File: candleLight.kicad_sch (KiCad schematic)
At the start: 43 parts, among them J1 USB_C_Receptacle_USB2.0, J2 Conn_Phoenix, J3 Conn_SWD, J4 Conn_IO, J5 Conn_BOOT0, J6 Conn_CAN_Jumper, J7 Conn_5V, U1 STM32F072C8Tx, U2 AMS1117-3.3, U3 TJA1051TK-3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

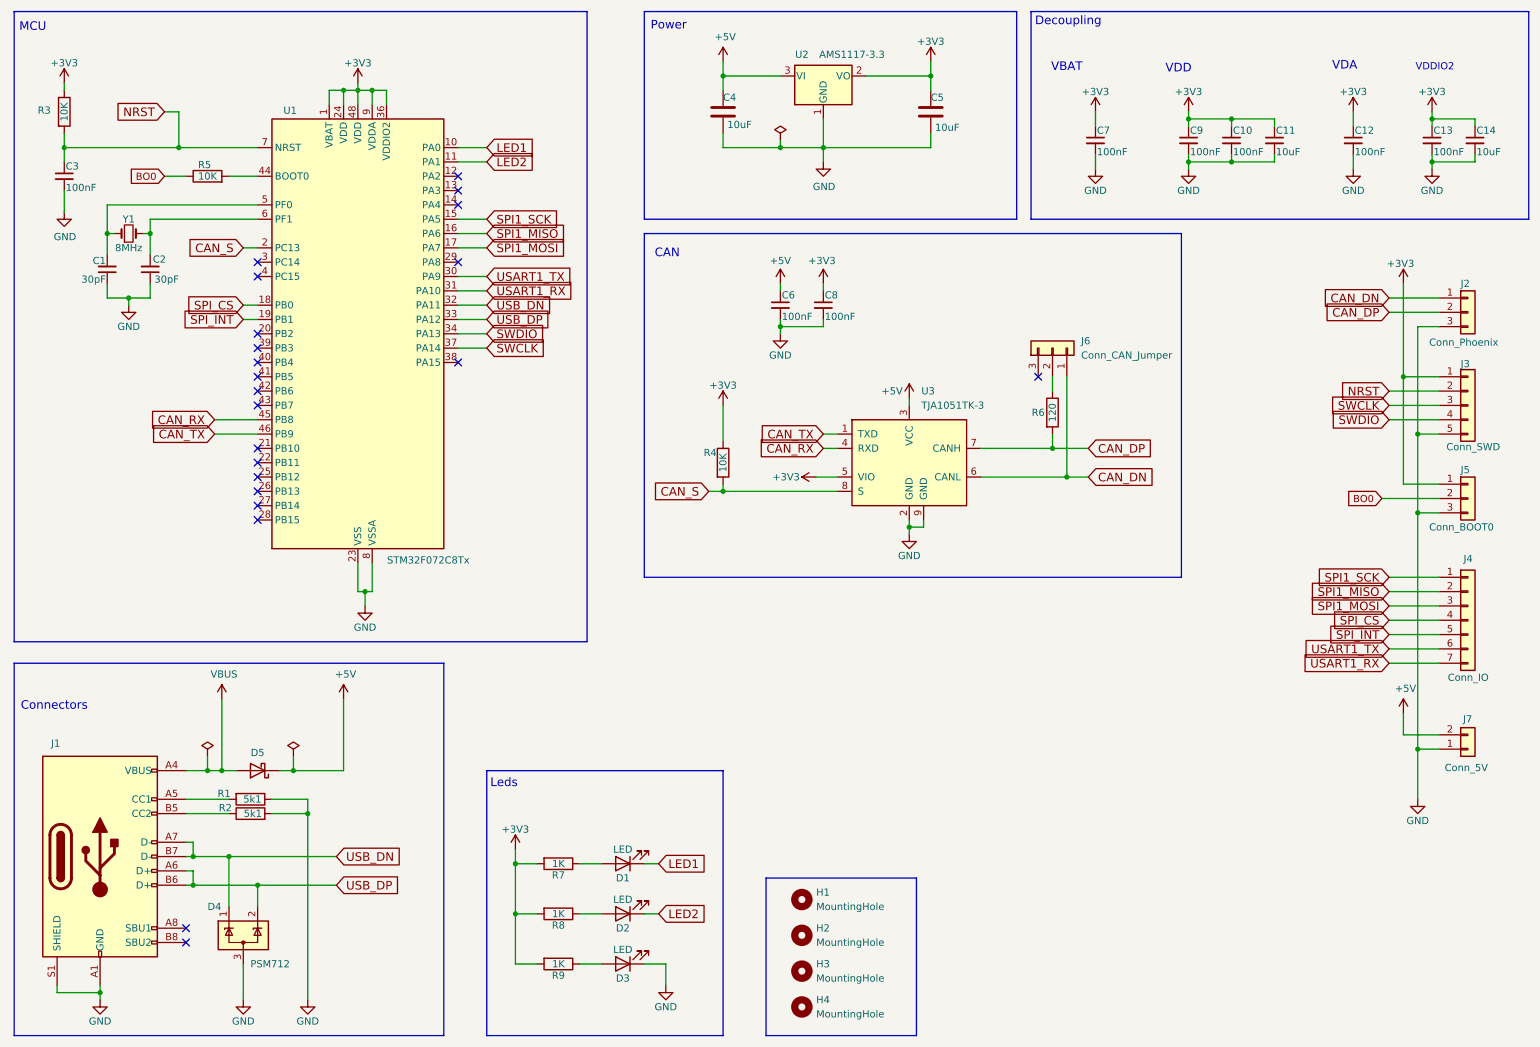
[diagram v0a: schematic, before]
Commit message: update schematic
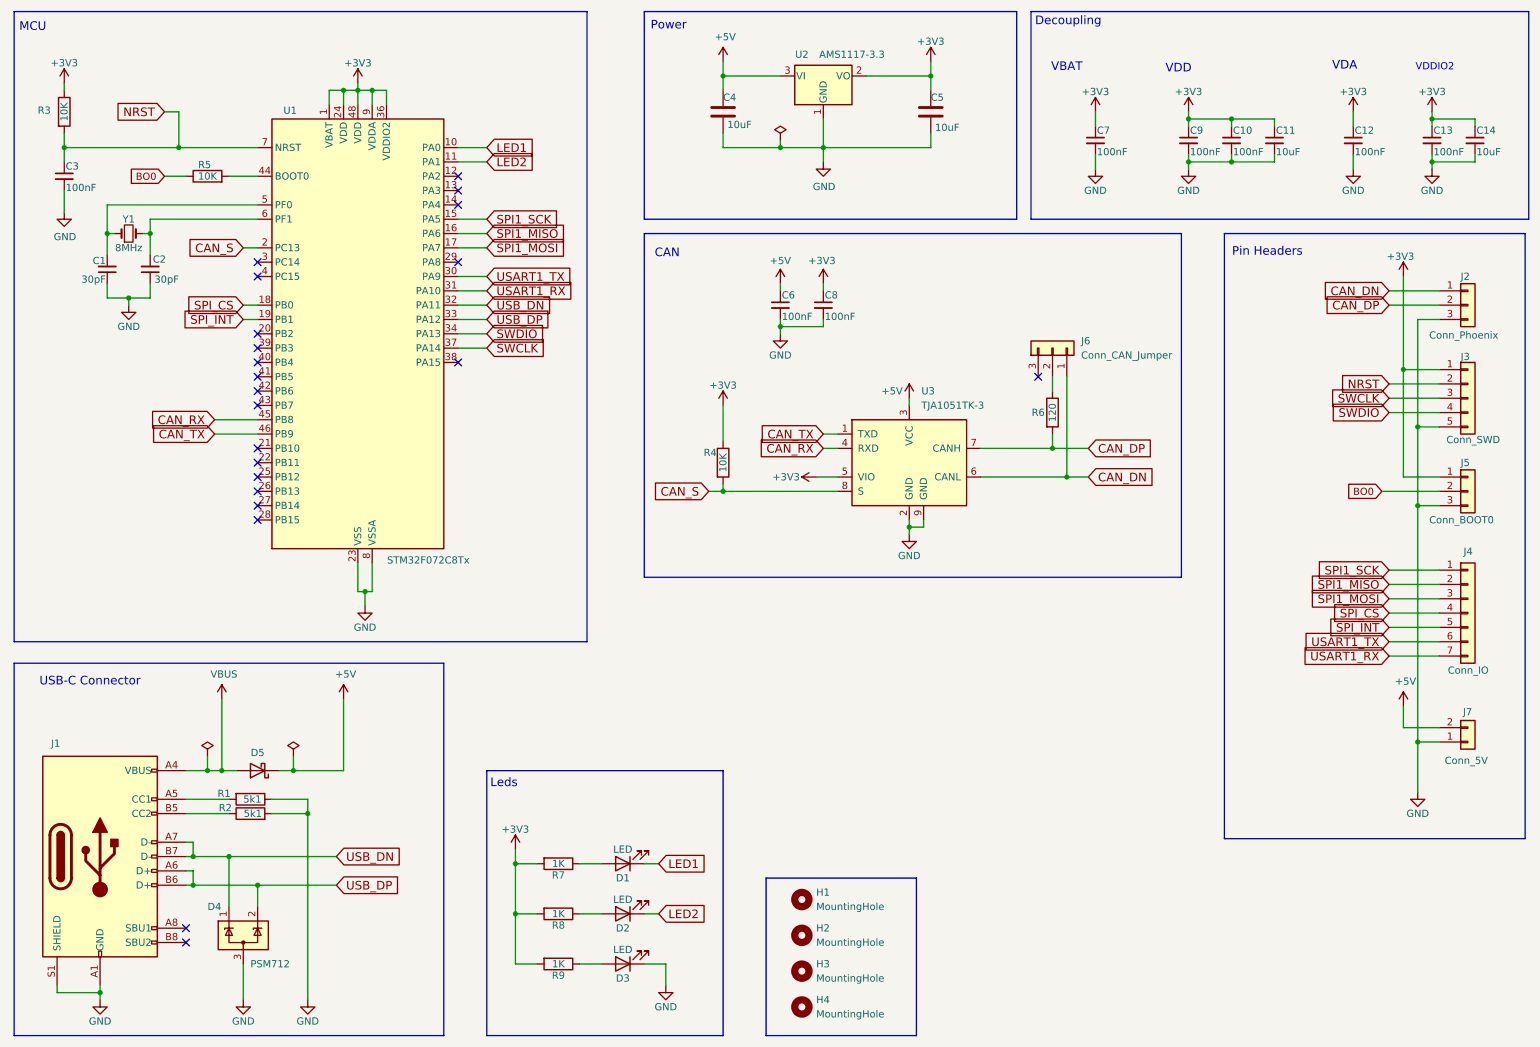
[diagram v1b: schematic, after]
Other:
- note added: "Pin Headers"
- note added: "USB-C Connector"
- note removed: "Connectors"
- moved on the sheet: J2, J3, J4, J5, J7
